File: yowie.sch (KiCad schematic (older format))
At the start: 0 parts

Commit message: Created STM32F405RG Part
Added to main schematics
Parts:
- added U?: STM32F405RG, symbol STM32F405RG
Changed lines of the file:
@@
 LIBS:contrib
 LIBS:valves
+LIBS:yowie_lib
+LIBS:yowie-cache
 EELAYER 25 0
 EELAYER END
@@
 Comment4 ""
 $EndDescr
+$Comp
+L STM32F405RG U?
+U 1 1 5652682C
+P 5850 1750
+F 0 "U?" H 5850 1750 60  0000 C CNN
+F 1 "STM32F405RG" H 5850 -1650 60  0000 C CNN
+F 2 "" H 5850 1750 60  0000 C CNN
+F 3 "" H 5850 1750 60  0000 C CNN
+	1    5850 1750
+	1    0    0    -1
+$EndComp
 $EndSCHEMATC

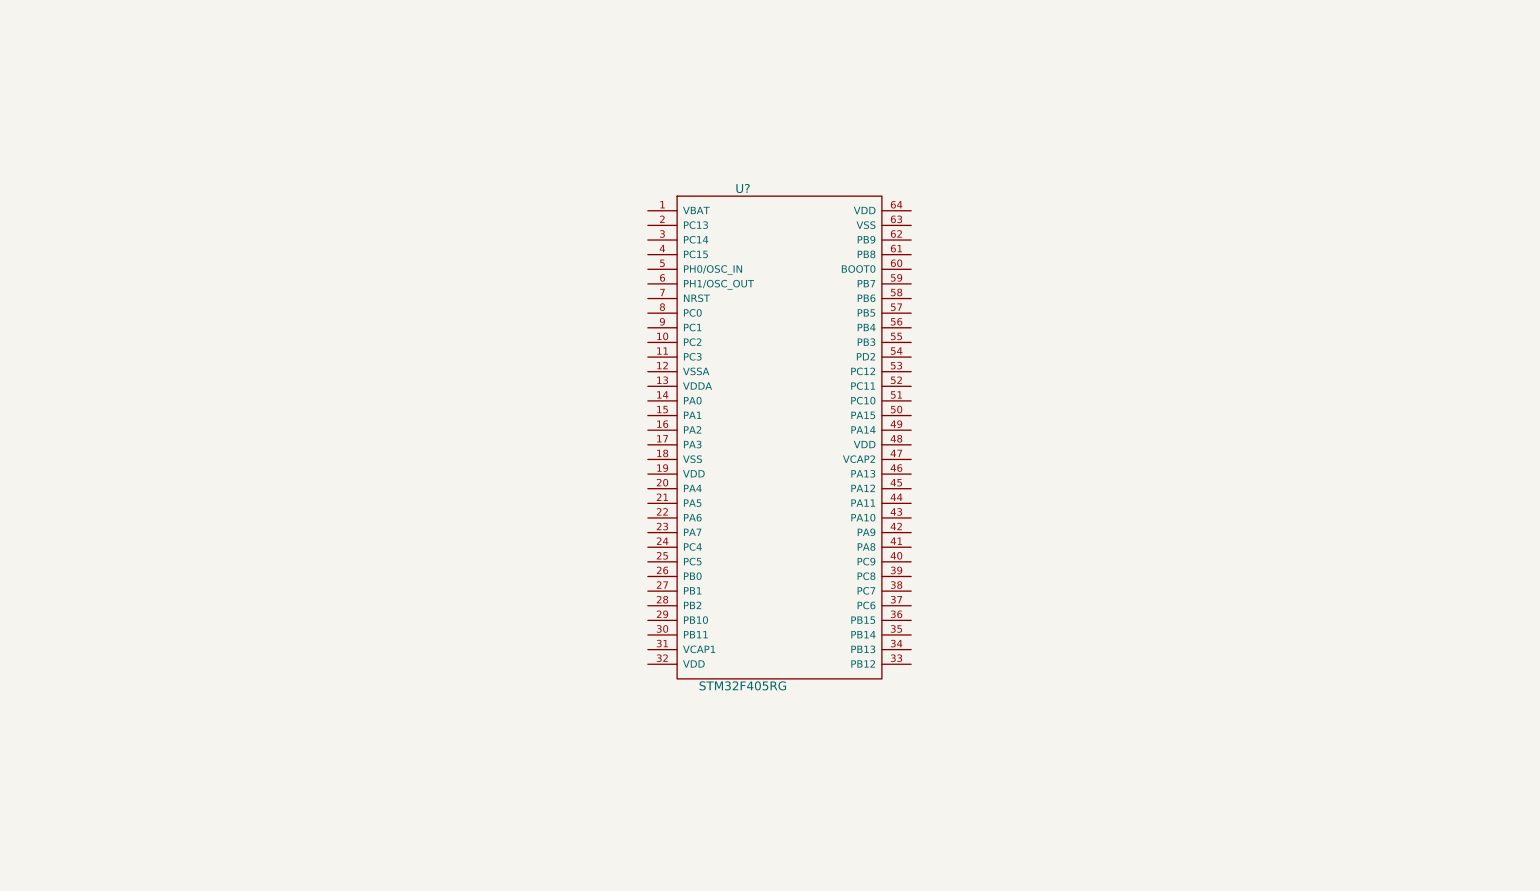
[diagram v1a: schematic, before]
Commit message: Added USB and supporting infrastructure
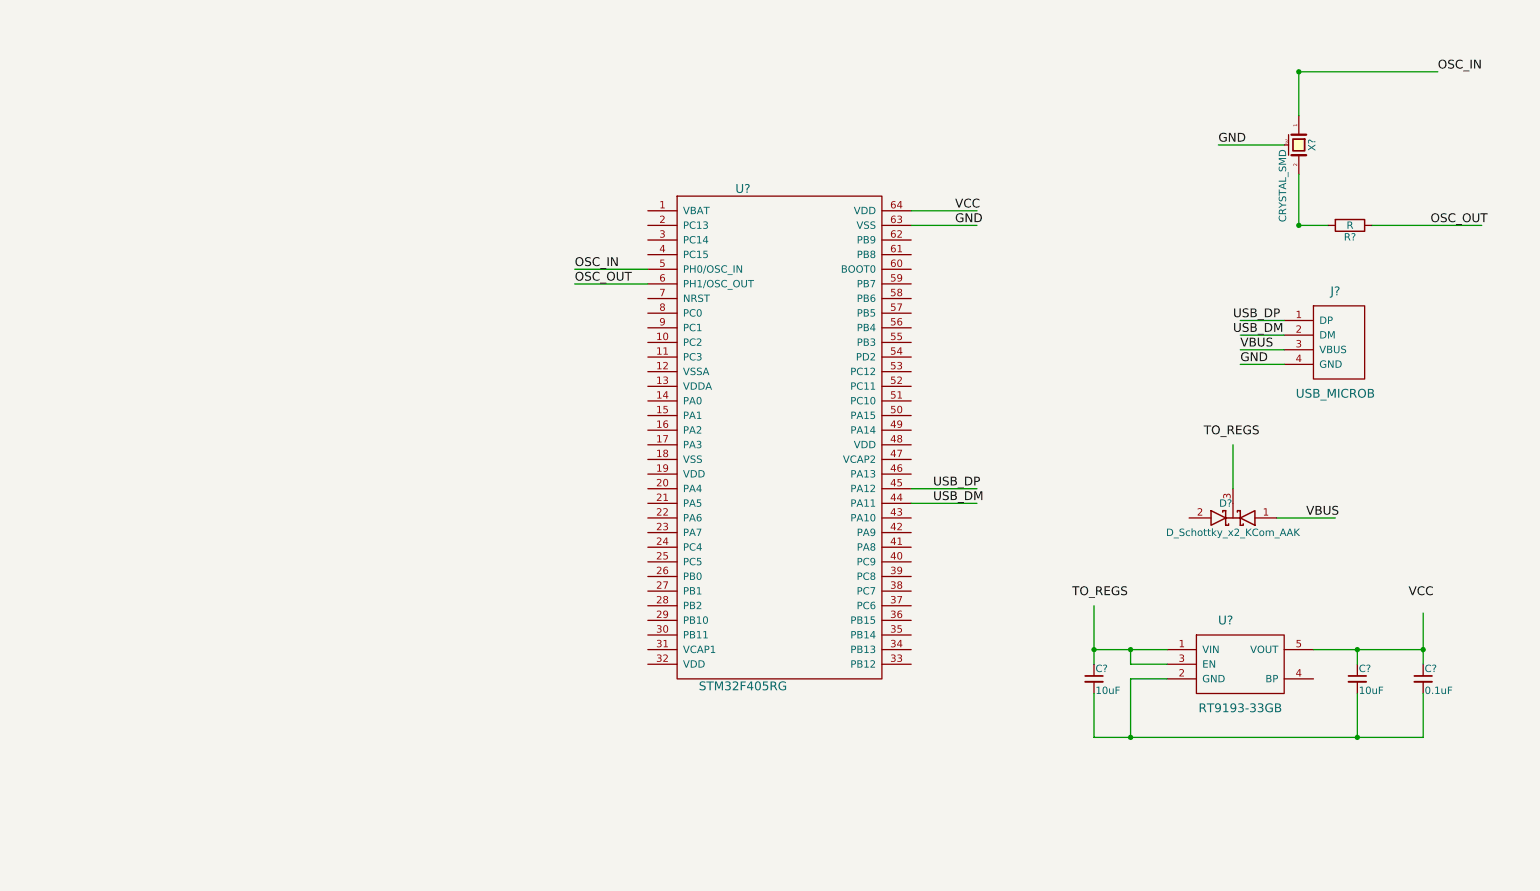
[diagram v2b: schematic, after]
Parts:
- added C? (x2): 10uF, symbol C_Small
- added C?: 0.1uF, symbol C_Small
- added D?: D_Schottky_x2_KCom_AAK, symbol D_Schottky_x2_KCom_AAK
- added J?: USB_MICROB, symbol USB_MICROB
- added R?: R, symbol R
- added U?: RT9193-33GB, symbol RT9193-33GB
- added X?: CRYSTAL_SMD, symbol CRYSTAL_SMD
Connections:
- net labels added: GND, OSC_IN, OSC_OUT, TO_REGS, USB_DM, USB_DP, VBUS, VCC
- wire segments 0 -> 31
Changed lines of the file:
@@
 	1    0    0    -1
 $EndComp
+$Comp
+L USB_MICROB J?
+U 1 1 56526A85
+P 9900 2450
+F 0 "J?" H 9900 2450 60  0000 C CNN
+F 1 "USB_MICROB" H 9900 1750 60  0000 C CNN
+F 2 "" H 9900 2450 60  0000 C CNN
+F 3 "" H 9900 2450 60  0000 C CNN
+	1    9900 2450
+	1    0    0    -1
+$EndComp
+$Comp
+L D_Schottky_x2_KCom_AAK D?
+U 1 1 56526B1B
+P 9200 4000
+F 0 "D?" H 9250 3900 50  0000 C CNN
+F 1 "D_Schottky_x2_KCom_AAK" H 9200 4100 50  0000 C CNN
+F 2 "" H 9200 4000 60  0000 C CNN
+F 3 "" H 9200 4000 60  0000 C CNN
+	1    9200 4000
+	-1   0    0    1
+$EndComp
+Text Label 9250 2850 0    60   ~ 0
+VBUS
+Text Label 9700 4000 0    60   ~ 0
+VBUS
+Text Label 9000 3450 0    60   ~ 0
+TO_REGS
+$Comp
+L RT9193-33GB U?
+U 1 1 56526EB8
+P 9150 4700
+F 0 "U?" H 9150 4700 60  0000 C CNN
+F 1 "RT9193-33GB" H 9250 4100 60  0000 C CNN
+F 2 "" H 9150 4700 60  0000 C CNN
+F 3 "" H 9150 4700 60  0000 C CNN
+	1    9150 4700
+	1    0    0    -1
+$EndComp
+$Comp
+L C_Small C?
+U 1 1 56526FDF
+P 8250 5100
+F 0 "C?" H 8260 5170 50  0000 L CNN
+F 1 "10uF" H 8260 5020 50  0000 L CNN
+F 2 "" H 8250 5100 60  0000 C CNN
+F 3 "" H 8250 5100 60  0000 C CNN
+	1    8250 5100
+	1    0    0    -1
+$EndComp
+$Comp
+L C_Small C?
+U 1 1 5652721E
+P 10050 5100
+F 0 "C?" H 10060 5170 50  0000 L CNN
+F 1 "10uF" H 10060 5020 50  0000 L CNN
+F 2 "" H 10050 5100 60  0000 C CNN
+F 3 "" H 10050 5100 60  0000 C CNN
+	1    10050 5100
+	1    0    0    -1
+$EndComp
+$Comp
+L C_Small C?
+U 1 1 5652725B
+P 10500 5100
+F 0 "C?" H 10510 5170 50  0000 L CNN
+F 1 "0.1uF" H 10510 5020 50  0000 L CNN
+F 2 "" H 10500 5100 60  0000 C CNN
+F 3 "" H 10500 5100 60  0000 C CNN
+	1    10500 5100
+	1    0    0    -1
+$EndComp
+Text Label 8100 4550 0    60   ~ 0
+TO_REGS
+Text Label 10400 4550 0    60   ~ 0
+VCC
+Text Label 9250 2950 0    60   ~ 0
+GND
+Text Label 7300 1900 0    60   ~ 0
+VCC
+Text Label 7300 2000 0    60   ~ 0
+GND
+Text Label 4700 2300 0    60   ~ 0
+OSC_IN
+Text Label 4700 2400 0    60   ~ 0
+OSC_OUT
+$Comp
+L R R?
+U 1 1 56527C00
+P 10000 2000
+F 0 "R?" V 10080 2000 50  0000 C CNN
+F 1 "R" V 10000 2000 50  0000 C CNN
+F 2 "" V 9930 2000 30  0000 C CNN
+F 3 "" H 10000 2000 30  0000 C CNN
+	1    10000 2000
+	0    1    1    0
+$EndComp
+Text Label 10600 950  0    60   ~ 0
+OSC_IN
+Text Label 10550 2000 0    60   ~ 0
+OSC_OUT
+Wire Wire Line
+	9200 3800 9200 3500
+Wire Wire Line
+	9500 4000 9900 4000
+Wire Wire Line
+	9550 2850 9250 2850
+Wire Wire Line
+	8250 4900 8750 4900
+Wire Wire Line
+	8250 4600 8250 5000
+Wire Wire Line
+	8750 5000 8500 5000
+Wire Wire Line
+	8500 5000 8500 4900
+Connection ~ 8500 4900
+Wire Wire Line
+	8750 5100 8500 5100
+Wire Wire Line
+	8500 5100 8500 5500
+Connection ~ 8250 4900
+Wire Wire Line
+	8250 5500 10500 5500
+Wire Wire Line
+	10500 5500 10500 5200
+Wire Wire Line
+	8250 5200 8250 5500
+Connection ~ 8500 5500
+Wire Wire Line
+	10050 5200 10050 5500
+Connection ~ 10050 5500
+Wire Wire Line
+	9750 4900 10500 4900
+Wire Wire Line
+	10500 4650 10500 5000
+Connection ~ 10500 4900
+Wire Wire Line
+	10050 5000 10050 4900
+Connection ~ 10050 4900
+Wire Wire Line
+	9550 2950 9250 2950
+Wire Wire Line
+	7000 1900 7450 1900
+Wire Wire Line
+	7000 2000 7450 2000
+Wire Wire Line
+	5200 2300 4700 2300
+Wire Wire Line
+	5200 2400 4700 2400
+Wire Wire Line
+	10150 2000 10900 2000
+Connection ~ 9650 950
+Connection ~ 9650 2000
+$Comp
+L CRYSTAL_SMD X?
+U 1 1 5653E728
+P 9650 1450
+F 0 "X?" H 9650 1540 50  0000 C CNN
+F 1 "CRYSTAL_SMD" H 9680 1340 50  0000 L CNN
+F 2 "" H 9650 1450 60  0000 C CNN
+F 3 "" H 9650 1450 60  0000 C CNN
+	1    9650 1450
+	0    1    1    0
+$EndComp
+Wire Wire Line
+	9650 950  9650 1250
+Wire Wire Line
+	9650 1650 9650 2000
+Wire Wire Line
+	9650 950  10600 950
+Wire Wire Line
+	9650 2000 9850 2000
+Wire Wire Line
+	9550 1450 9100 1450
+Text Label 9100 1450 0    60   ~ 0
+GND
+Wire Wire Line
+	7000 3900 7450 3900
+Wire Wire Line
+	7000 3800 7450 3800
+Text Label 7150 3900 0    60   ~ 0
+USB_DM
+Text Label 7150 3800 0    60   ~ 0
+USB_DP
+Wire Wire Line
+	9550 2750 9250 2750
+Wire Wire Line
+	9550 2650 9250 2650
+Text Label 9200 2750 0    60   ~ 0
+USB_DM
+Text Label 9200 2650 0    60   ~ 0
+USB_DP
 $EndSCHEMATC

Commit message: Added VCC_IN, RC in, ESC out
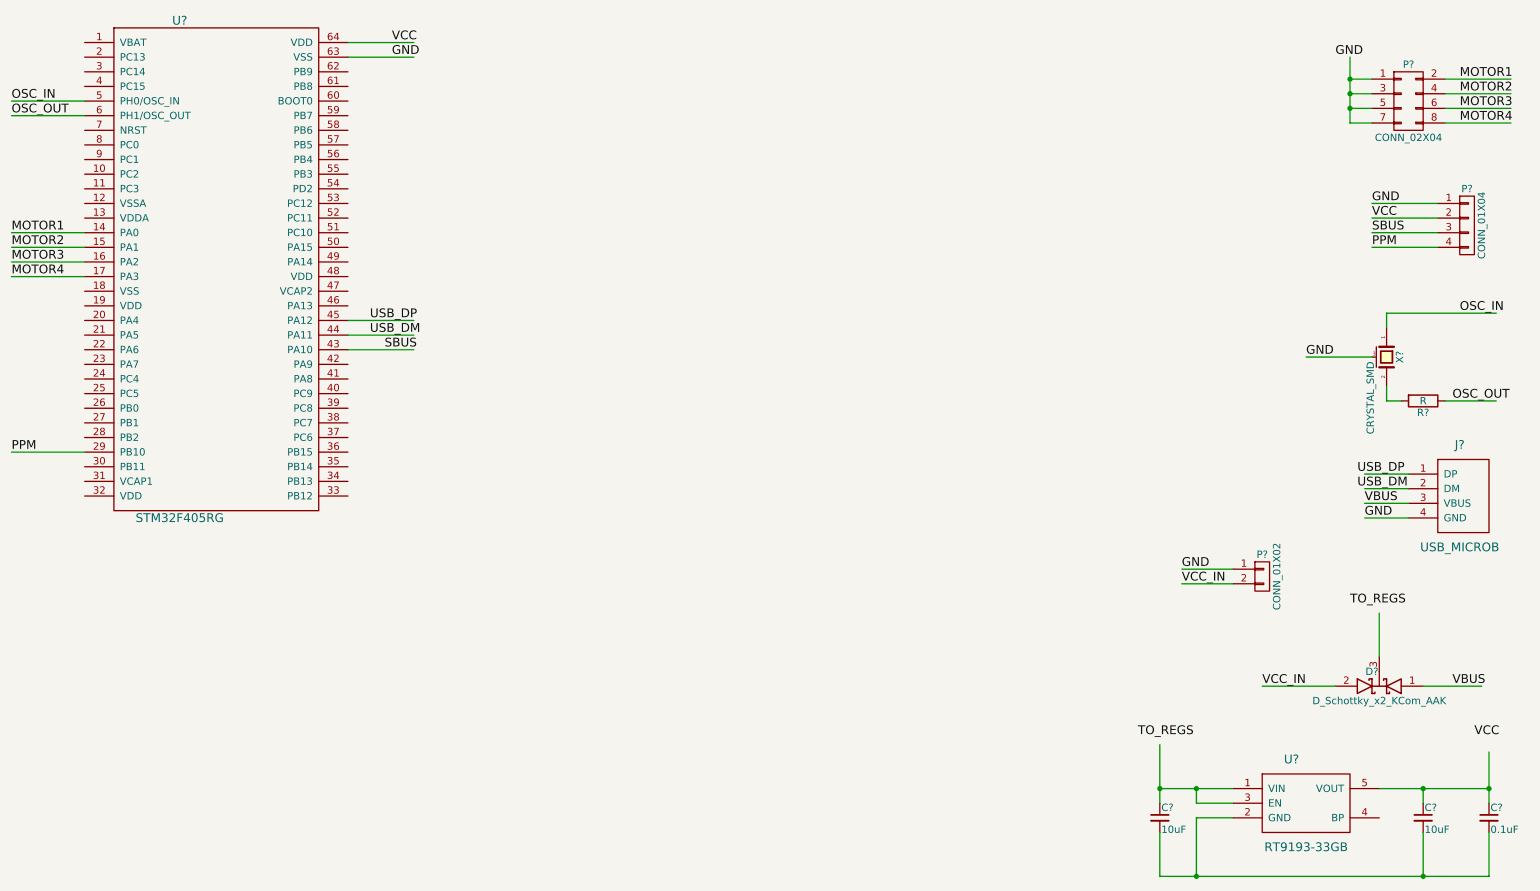
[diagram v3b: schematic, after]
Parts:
- added P?: CONN_01X02, symbol CONN_01X02
- added P?: CONN_01X04, symbol CONN_01X04
- added P?: CONN_02X04, symbol CONN_02X04
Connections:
- net labels added: MOTOR1, MOTOR2, MOTOR3, MOTOR4, PPM, SBUS, VCC_IN
- wire segments 31 -> 53
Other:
- moved on the sheet: C?, D?, J?, R?, U?, X?
